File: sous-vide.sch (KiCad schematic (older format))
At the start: 25 parts, among them J2 Conn_01x02, J3 Conn_01x02, J5 Conn_01x02, Q1 2N3904, SW1 SW_Push_Dual, SW2 SW_Push_Dual, U1 node_mcu1.0, U2 RAC01, U3 G5LE, U4 LCD_Backpack, U5 P090S-04F20BR10K

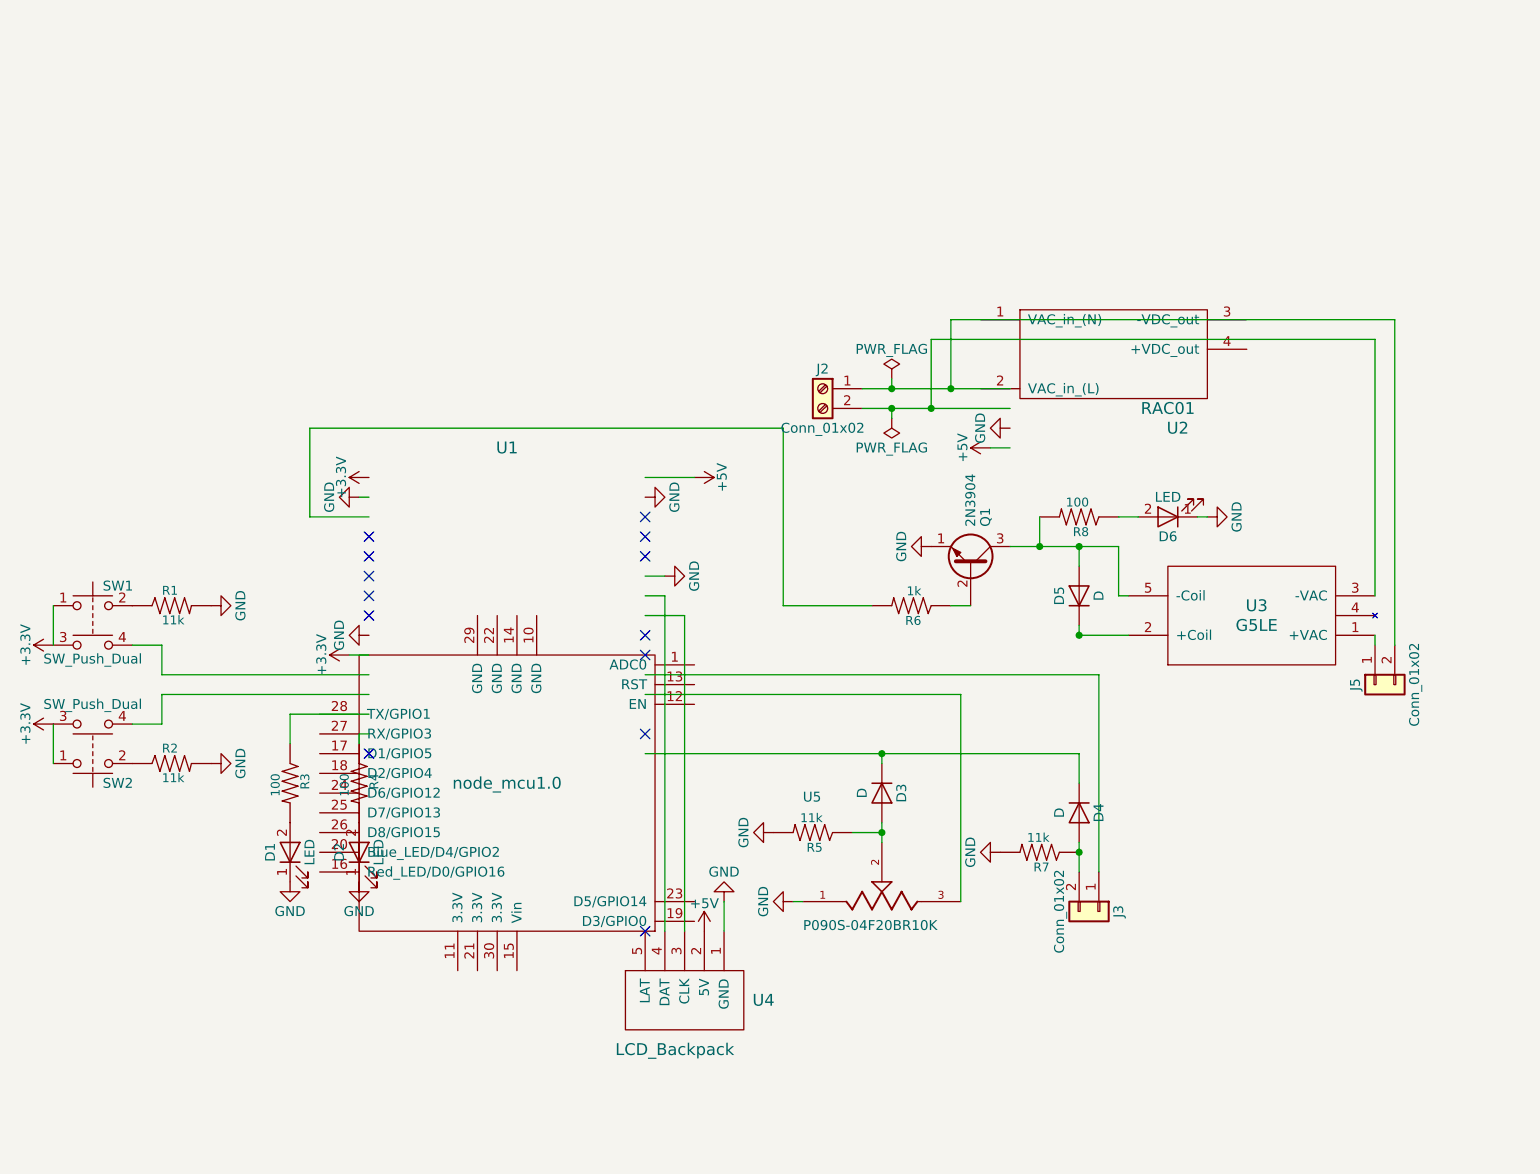
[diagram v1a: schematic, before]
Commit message: started testing pins for GPIO
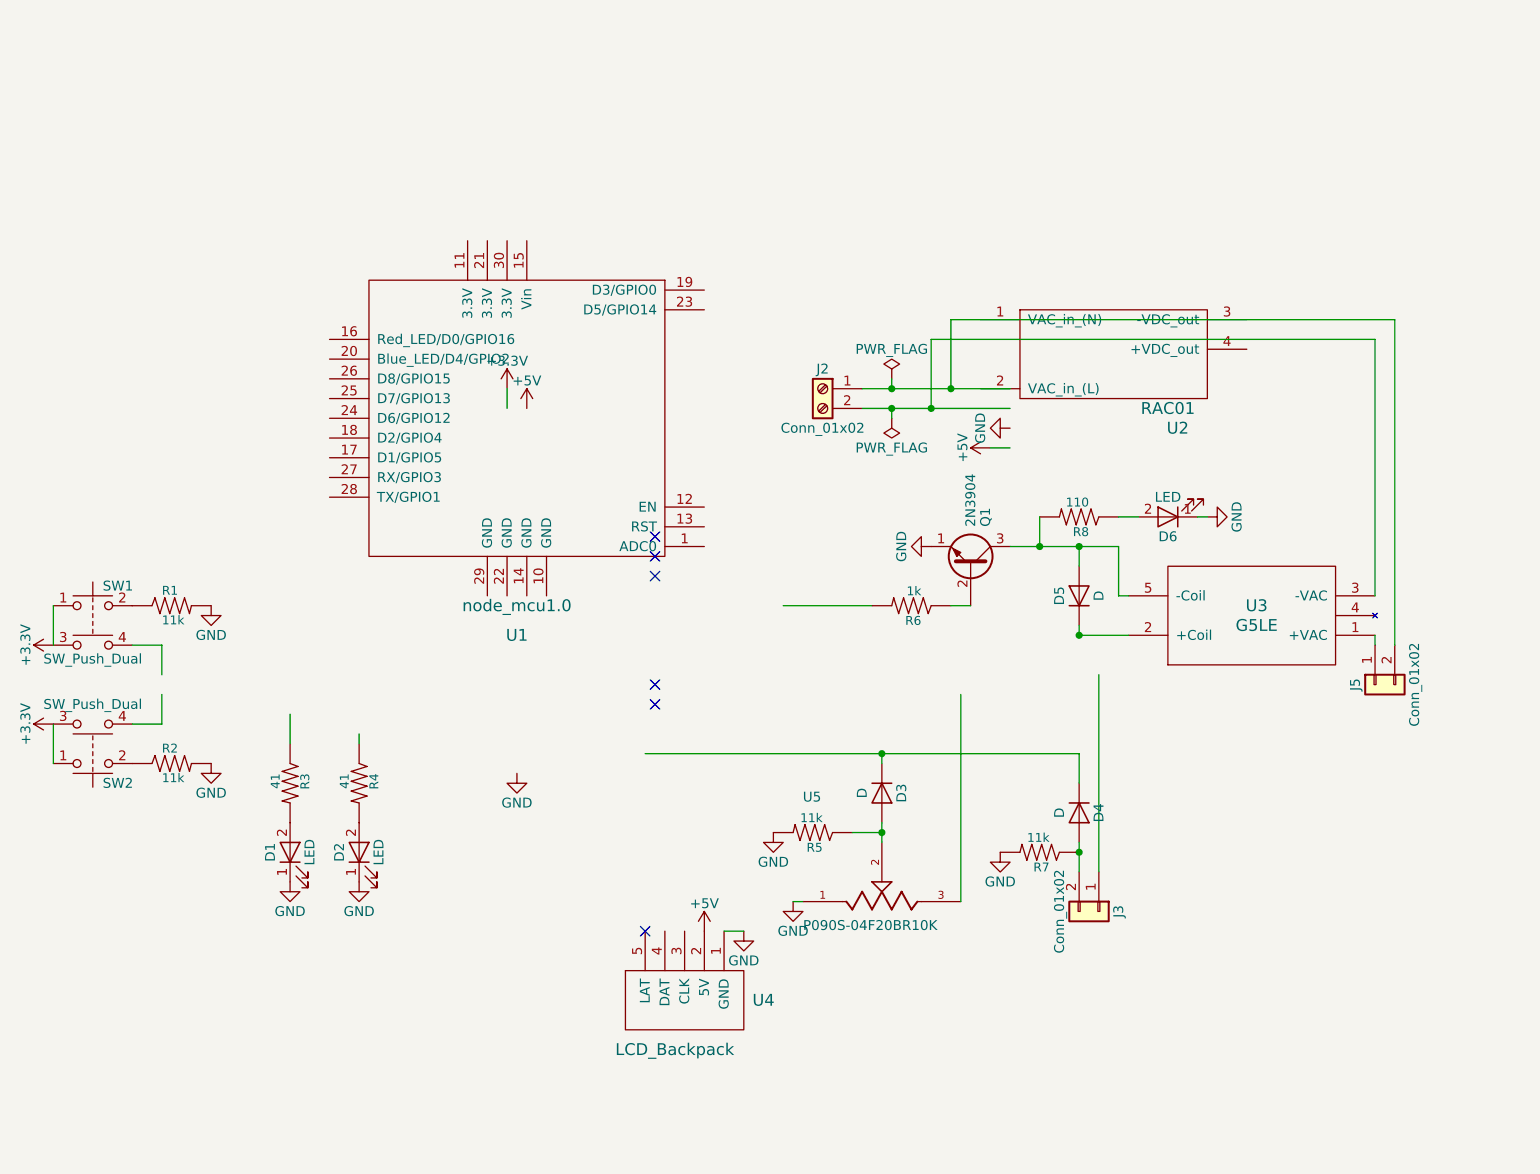
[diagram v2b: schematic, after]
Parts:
- R3, R4: value 100 -> 41
- R8: value 100 -> 110
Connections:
- wire segments 60 -> 43
- no-connect marks 13 -> 6
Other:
- moved on the sheet: U1
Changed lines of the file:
@@
 L GND #PWR01
 U 1 1 5A456926
-P 5050 5200
-F 0 "#PWR01" H 5050 4950 50  0001 C CNN
-F 1 "GND" H 5050 5050 50  0000 C CNN
-F 2 "" H 5050 5200 50  0001 C CNN
-F 3 "" H 5050 5200 50  0001 C CNN
-	1    5050 5200
-	-1   0    0    1
+P 5150 5350
+F 0 "#PWR01" H 5150 5100 50  0001 C CNN
+F 1 "GND" H 5150 5200 50  0000 C CNN
+F 2 "" H 5150 5350 50  0001 C CNN
+F 3 "" H 5150 5350 50  0001 C CNN
+	1    5150 5350
+	1    0    0    -1
 $EndComp
 $Comp
 L node_mcu1.0 U1
 U 1 1 5A457536
-P 3950 4650
-F 0 "U1" H 3950 2900 60  0000 C CNN
-F 1 "node_mcu1.0" H 3950 4600 60  0000 C CNN
-F 2 "custom:NodeMCU_1_0" H 3700 4600 60  0001 C CNN
-F 3 "" H 3700 4600 60  0001 C CNN
-	1    3950 4650
-	-1   0    0    1
+P 4000 2750
+F 0 "U1" H 4000 1650 60  0000 C CNN
+F 1 "node_mcu1.0" H 4000 1800 60  0000 C CNN
+F 2 "custom:NodeMCU_1_0" H 3750 2700 60  0001 C CNN
+F 3 "" H 3750 2700 60  0001 C CNN
+	1    4000 2750
+	-1   0    0    -1
 $EndComp
 $Comp
@@
 F 3 "" H 5400 5200 50  0001 C CNN
 	1    5400 5200
-	0    1    1    0
+	1    0    0    -1
 $EndComp
 $Comp
@@
 F 3 "" H 5300 4850 50  0001 C CNN
 	1    5300 4850
-	0    1    1    0
+	1    0    0    -1
 $EndComp
 $Comp
@@
 F 3 "" H 6450 4950 50  0001 C CNN
 	1    6450 4950
-	0    1    1    0
+	1    0    0    -1
 $EndComp
 $Comp
@@
 $EndComp
 Wire Wire Line
-	6950 4050 4650 4050
-Wire Wire Line
-	2950 2800 2950 3250
-Wire Wire Line
-	2950 3250 3250 3250
-Wire Wire Line
 	6850 4900 6850 5050
-Wire Wire Line
-	4650 4150 6250 4150
-Wire Wire Line
-	4750 5350 4750 3650
-Wire Wire Line
-	4750 3650 4650 3650
-Wire Wire Line
-	4850 5350 4850 3750
-Wire Wire Line
-	4850 3750 4650 3750
 Wire Wire Line
 	6850 4950 6850 4950
@@
 	0    1    1    0
 $EndComp
-Wire Wire Line
-	5350 2800 2950 2800
-Wire Wire Line
-	5350 2800 5350 3700
 Wire Wire Line
 	6500 3400 7050 3400
@@
 F 3 "" H 2450 4500 50  0001 C CNN
 	1    2450 4500
-	0    -1   -1   0
+	1    0    0    -1
 $EndComp
 Wire Wire Line
@@
 P 6850 3250
 F 0 "R8" H 6800 3300 45  0000 L BNN
-F 1 "100" H 6800 3150 45  0000 L BNN
+F 1 "110" H 6800 3150 45  0000 L BNN
 F 2 "Resistors_THT:R_Axial_DIN0204_L3.6mm_D1.6mm_P7.62mm_Horizontal" H 6850 3400 20  0001 C CNN
 F 3 "" H 6850 3250 60  0001 C CNN
@@
 P 3200 4600
 F 0 "R4" H 3150 4650 45  0000 L BNN
-F 1 "100" H 3150 4500 45  0000 L BNN
+F 1 "41" H 3150 4500 45  0000 L BNN
 F 2 "Resistors_THT:R_Axial_DIN0204_L3.6mm_D1.6mm_P7.62mm_Horizontal" H 3200 4750 20  0001 C CNN
 F 3 "" H 3200 4600 60  0001 C CNN
@@
 Wire Wire Line
 	3200 4400 3200 4350
-Wire Wire Line
-	3200 4350 3250 4350
 $Comp
 L RESISTOR0402 R2
@@
 F 3 "" H 2450 3700 50  0001 C CNN
 	1    2450 3700
-	0    -1   -1   0
+	1    0    0    -1
 $EndComp
 Wire Wire Line
@@
 Wire Wire Line
 	2200 4300 2200 4150
-Wire Wire Line
-	2200 4150 3250 4150
-Wire Wire Line
-	2200 4050 3250 4050
 $Comp
 L RESISTOR0402 R3
@@
 P 2850 4600
 F 0 "R3" H 2800 4650 45  0000 L BNN
-F 1 "100" H 2800 4500 45  0000 L BNN
+F 1 "41" H 2800 4500 45  0000 L BNN
 F 2 "Resistors_THT:R_Axial_DIN0204_L3.6mm_D1.6mm_P7.62mm_Horizontal" H 2850 4750 20  0001 C CNN
 F 3 "" H 2850 4600 60  0001 C CNN
@@
 	2850 4400 2850 4250
 Wire Wire Line
-	2850 4250 3250 4250
-Wire Wire Line
 	8350 3900 8350 3850
 Wire Wire Line
@@
 Connection ~ 6100 2700
 Connection ~ 6200 2600
-NoConn ~ 3250 4450
-NoConn ~ 3250 3750
-NoConn ~ 3250 3650
-NoConn ~ 3250 3550
-NoConn ~ 3250 3450
-NoConn ~ 3250 3350
-NoConn ~ 4650 3250
-NoConn ~ 4650 3350
-NoConn ~ 4650 3450
-$Comp
-L GND #PWR011
-U 1 1 5A4713DB
-P 4750 3550
-F 0 "#PWR011" H 4750 3300 50  0001 C CNN
-F 1 "GND" H 4750 3400 50  0000 C CNN
-F 2 "" H 4750 3550 50  0001 C CNN
-F 3 "" H 4750 3550 50  0001 C CNN
-	1    4750 3550
-	0    -1   -1   0
-$EndComp
-$Comp
-L GND #PWR012
-U 1 1 5A471499
-P 3200 3150
-F 0 "#PWR012" H 3200 2900 50  0001 C CNN
-F 1 "GND" H 3200 3000 50  0000 C CNN
-F 2 "" H 3200 3150 50  0001 C CNN
-F 3 "" H 3200 3150 50  0001 C CNN
-	1    3200 3150
-	0    1    1    0
-$EndComp
-NoConn ~ 4650 3850
-NoConn ~ 4650 3950
-NoConn ~ 4650 4350
-Wire Wire Line
-	4650 3550 4750 3550
-Wire Wire Line
-	3250 3150 3200 3150
 $Comp
 L GND #PWR013
@@
 F 3 "" H 6500 2800 50  0001 C CNN
 	1    6500 2800
-	0    1    1    0
-$EndComp
-$Comp
-L GND #PWR014
-U 1 1 5A475347
-P 4650 3150
-F 0 "#PWR014" H 4650 2900 50  0001 C CNN
-F 1 "GND" H 4650 3000 50  0000 C CNN
-F 2 "" H 4650 3150 50  0001 C CNN
-F 3 "" H 4650 3150 50  0001 C CNN
-	1    4650 3150
-	0    -1   -1   0
-$EndComp
-Wire Wire Line
-	4650 3050 4900 3050
-$Comp
-L GND #PWR015
-U 1 1 5A478DA6
-P 3250 3850
-F 0 "#PWR015" H 3250 3600 50  0001 C CNN
-F 1 "GND" H 3250 3700 50  0000 C CNN
-F 2 "" H 3250 3850 50  0001 C CNN
-F 3 "" H 3250 3850 50  0001 C CNN
-	1    3250 3850
 	0    1    1    0
 $EndComp
@@
 $EndComp
 $Comp
-L +5V #PWR018
-U 1 1 5A46409D
-P 4900 3050
-F 0 "#PWR018" H 4900 2900 50  0001 C CNN
-F 1 "+5V" H 4900 3190 50  0000 C CNN
-F 2 "" H 4900 3050 50  0001 C CNN
-F 3 "" H 4900 3050 50  0001 C CNN
-	1    4900 3050
-	0    1    1    0
-$EndComp
-$Comp
 L +5V #PWR019
 U 1 1 5A4640F9
@@
 $EndComp
 Wire Wire Line
-	5050 5200 5050 5350
+	5150 5350 5050 5350
 Connection ~ 5900 2600
 $Comp
@@
 Wire Wire Line
 	1650 4300 1650 4500
-$Comp
-L +3.3V #PWR023
-U 1 1 5A476C4E
-P 3250 3050
-F 0 "#PWR023" H 3250 2900 50  0001 C CNN
-F 1 "+3.3V" H 3250 3190 50  0000 C CNN
-F 2 "" H 3250 3050 50  0001 C CNN
-F 3 "" H 3250 3050 50  0001 C CNN
-	1    3250 3050
-	0    -1   -1   0
-$EndComp
-$Comp
-L +3.3V #PWR024
-U 1 1 5A4637BE
-P 3150 3950
-F 0 "#PWR024" H 3150 3800 50  0001 C CNN
-F 1 "+3.3V" H 3150 4090 50  0000 C CNN
-F 2 "" H 3150 3950 50  0001 C CNN
-F 3 "" H 3150 3950 50  0001 C CNN
-	1    3150 3950
-	0    -1   -1   0
-$EndComp
-Wire Wire Line
-	3150 3950 3250 3950
 $Comp
 L P090S-04F20BR10K U5
@@
 	1    0    0    -1
 $EndComp
+$Comp
+L +5V #PWR?
+U 1 1 5A48311D
+P 4050 2700
+F 0 "#PWR?" H 4050 2550 50  0001 C CNN
+F 1 "+5V" H 4050 2840 50  0000 C CNN
+F 2 "" H 4050 2700 50  0001 C CNN
+F 3 "" H 4050 2700 50  0001 C CNN
+	1    4050 2700
+	1    0    0    -1
+$EndComp
+$Comp
+L +3.3V #PWR?
+U 1 1 5A483163
+P 3950 2600
+F 0 "#PWR?" H 3950 2450 50  0001 C CNN
+F 1 "+3.3V" H 3950 2740 50  0000 C CNN
+F 2 "" H 3950 2600 50  0001 C CNN
+F 3 "" H 3950 2600 50  0001 C CNN
+	1    3950 2600
+	1    0    0    -1
+$EndComp
+Wire Wire Line
+	3950 2600 3950 2700
+$Comp
+L GND #PWR?
+U 1 1 5A48356C
+P 4000 4550
+F 0 "#PWR?" H 4000 4300 50  0001 C CNN
+F 1 "GND" H 4000 4400 50  0000 C CNN
+F 2 "" H 4000 4550 50  0001 C CNN
+F 3 "" H 4000 4550 50  0001 C CNN
+	1    4000 4550
+	1    0    0    -1
+$EndComp
+NoConn ~ 4700 4100
+NoConn ~ 4700 4200
+NoConn ~ 4700 3350
+NoConn ~ 4700 3450
+NoConn ~ 4700 3550
 $EndSCHEMATC

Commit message: redo entire schematic and layout
now complete with danger zone!
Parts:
- removed R1, R2: 11k, Resistors_THT:R_Axial_DIN0204_L3.6mm_D1.6mm_P7.62mm_Horizontal, symbol RESISTOR0402
- renumbered D3 to D1, D5 to D2, D6 to D3, D2 to D5, D1 to D6, J5 to J1, R8 to R1, R5 to R2, R6 to R3, R3 to R5, R7 to R6, U3 to U1, U1 to U3, U5 to U4, U4 to U5
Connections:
- net labels added: A0, BLUE_LED, CLK, DAT, RED_LED, SW1, SW2, THERMISTOR, UESR_POT
- wire segments 43 -> 60
- no-connect marks 6 -> 9
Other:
- note added: "Danger Zone"
- moved on the sheet: D1, D2, D3, D4, D5, D6, J1, J2, J3, Q1, R1, R2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

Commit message: fix DRC issues
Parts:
- U4: value P090S-04F20BR10K -> P090S
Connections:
- net labels removed: +3.3V
- wire segments 60 -> 44
- no-connect marks 9 -> 12
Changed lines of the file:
@@
 P 6500 5900
 F 0 "U4" H 6250 5950 50  0000 L BNN
-F 1 "P090S-04F20BR10K" H 6100 5750 50  0000 L BNN
+F 1 "P090S" H 6100 5750 50  0000 L BNN
 F 2 "P090S-04F20BR10K:TRIM_P090S-04F20BR10K" H 6500 5900 50  0001 L BNN
 F 3 "P090S-04F20BR10K" H 6500 5900 50  0001 L BNN
@@
 $EndComp
 $Comp
-L node_mcu1.0 U3
-U 1 1 5A457536
-P 5400 4200
-F 0 "U3" H 5250 4050 60  0000 C CNN
-F 1 "node_mcu1.0" H 5250 4200 60  0000 C CNN
-F 2 "custom:NodeMCU_1_0" H 5150 4150 60  0001 C CNN
-F 3 "" H 5150 4150 60  0001 C CNN
-	1    5400 4200
-	1    0    0    -1
-$EndComp
-$Comp
 L GND #PWR014
 U 1 1 5A485E99
@@
 NoConn ~ 6350 4500
 $Comp
-L +3.3V #PWR016
-U 1 1 5A483163
-P 5450 3250
-F 0 "#PWR016" H 5450 3100 50  0001 C CNN
-F 1 "+3.3V" H 5450 3390 50  0000 C CNN
-F 2 "" H 5450 3250 50  0001 C CNN
-F 3 "" H 5450 3250 50  0001 C CNN
-	1    5450 3250
-	1    0    0    -1
-$EndComp
-$Comp
-L +5V #PWR017
+L +5V #PWR016
 U 1 1 5A490EFE
 P 5200 3300
-F 0 "#PWR017" H 5200 3150 50  0001 C CNN
+F 0 "#PWR016" H 5200 3150 50  0001 C CNN
 F 1 "+5V" H 5200 3440 50  0000 C CNN
 F 2 "" H 5200 3300 50  0001 C CNN
@@
 $EndComp
 $Comp
-L +5V #PWR018
+L +5V #PWR017
 U 1 1 5A491092
 P 6050 1300
-F 0 "#PWR018" H 6050 1150 50  0001 C CNN
+F 0 "#PWR017" H 6050 1150 50  0001 C CNN
 F 1 "+5V" H 6050 1440 50  0000 C CNN
 F 2 "" H 6050 1300 50  0001 C CNN
@@
 $EndComp
 $Comp
-L +5V #PWR019
+L +5V #PWR018
 U 1 1 5A4912B7
 P 7800 3800
-F 0 "#PWR019" H 7800 3650 50  0001 C CNN
+F 0 "#PWR018" H 7800 3650 50  0001 C CNN
 F 1 "+5V" H 7800 3940 50  0000 C CNN
 F 2 "" H 7800 3800 50  0001 C CNN
@@
 Text Label 4250 3550 0    60   ~ 0
 SW1
-Text Label 4250 4150 0    60   ~ 0
+Text Label 4250 3950 3    60   ~ 0
 SW2
 Wire Wire Line
-	6950 5450 7200 5450
-Wire Wire Line
-	7200 5450 7300 5450
+	6950 5450 7300 5450
 Connection ~ 7200 5450
 Wire Wire Line
 	5600 1400 6050 1400
 Wire Wire Line
-	6050 1300 6050 1400
-Wire Wire Line
-	6050 1400 6050 1450
-Wire Wire Line
-	5650 1850 6050 1850
-Wire Wire Line
-	6050 1850 6250 1850
-Wire Wire Line
-	6050 1750 6050 1850
-Wire Wire Line
-	6050 1850 6050 1900
+	6050 1300 6050 1450
+Wire Wire Line
+	5650 1850 6250 1850
+Wire Wire Line
+	6050 1750 6050 1900
 Connection ~ 6050 1400
 Wire Wire Line
@@
 	3650 2150 3650 2200
 Wire Wire Line
-	6100 5900 6150 5900
-Wire Wire Line
-	6150 5900 6200 5900
-Wire Wire Line
-	5450 3300 5450 3250
+	6100 5900 6200 5900
 Wire Wire Line
 	3550 3550 3700 3550
@@
 Wire Wire Line
 	4100 3550 4450 3550
-Wire Wire Line
-	4450 3550 4450 3700
-Wire Wire Line
-	4450 3800 4450 4150
-Wire Wire Line
-	4450 4150 4100 4150
 Wire Wire Line
 	6350 3550 6350 3800
@@
 Connection ~ 6150 5900
 Wire Wire Line
-	4450 5450 5800 5450
-Wire Wire Line
-	5800 5450 6650 5450
+	4450 5450 6650 5450
 Wire Wire Line
 	4450 5450 4450 4850
@@
 	6450 4000 6350 4000
 Wire Wire Line
-	3500 2200 3650 2200
-Wire Wire Line
-	3650 2200 4000 2200
-Wire Wire Line
-	4000 2200 4350 2200
+	3500 2200 4350 2200
 Wire Wire Line
 	4000 2200 4000 1500
 Wire Wire Line
-	4200 1600 4200 2300
-Wire Wire Line
-	4200 2300 4200 2550
+	4200 1600 4200 2550
 Wire Wire Line
 	4200 1600 4350 1600
 Wire Wire Line
-	3500 2300 3650 2300
-Wire Wire Line
-	3650 2300 4200 2300
+	3500 2300 4200 2300
 Wire Wire Line
 	3500 1400 4350 1400
@@
 UESR_POT
 Wire Wire Line
-	5450 3300 5550 3300
-Wire Wire Line
-	5550 3300 5650 3300
-Connection ~ 5550 3300
-Wire Wire Line
-	5250 5100 5350 5100
-Wire Wire Line
-	5350 5100 5400 5100
-Wire Wire Line
-	5400 5100 5450 5100
-Wire Wire Line
-	5450 5100 5550 5100
+	5250 5100 5550 5100
 Connection ~ 5350 5100
 Connection ~ 5400 5100
 Connection ~ 5450 5100
+Wire Wire Line
+	4100 4150 4250 4150
+Wire Wire Line
+	4250 4150 4250 3650
+Wire Wire Line
+	4250 3650 4450 3650
+$Comp
+L node_mcu1.0 U3
+U 1 1 5A457536
+P 5400 4200
+F 0 "U3" H 5250 4050 60  0000 C CNN
+F 1 "node_mcu1.0" H 5250 4200 60  0000 C CNN
+F 2 "custom:NodeMCU_1_0" H 5150 4150 60  0001 C CNN
+F 3 "" H 5150 4150 60  0001 C CNN
+	1    5400 4200
+	1    0    0    -1
+$EndComp
+NoConn ~ 5450 3300
+NoConn ~ 5550 3300
+NoConn ~ 5650 3300
 $EndSCHEMATC

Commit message: fix resistor footprints
 - add dashed line
 - fix pot to use through hole mounting
 - checked everything for footprint errors
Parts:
- R1, R2, R6: footprint Resistors_THT:R_Axial_DIN0204_L3.6mm_D1.6mm_P7.62mm_Horizontal -> Resistors_THT:R_Axial_DIN0207_L6.3mm_D2.5mm_P10.16mm_Horizontal
- R3: value 1k -> 1.1k; footprint Resistors_THT:R_Axial_DIN0204_L3.6mm_D1.6mm_P7.62mm_Horizontal -> Resistors_THT:R_Axial_DIN0207_L6.3mm_D2.5mm_P10.16mm_Horizontal
- R4, R5: value 41 -> 43; footprint Resistors_THT:R_Axial_DIN0204_L3.6mm_D1.6mm_P7.62mm_Horizontal -> Resistors_THT:R_Axial_DIN0207_L6.3mm_D2.5mm_P10.16mm_Horizontal
- U4: footprint P090S-04F20BR10K:TRIM_P090S-04F20BR10K -> custom:P090S-THT_MNT
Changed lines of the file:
@@
 F 0 "R2" H 6100 6150 45  0000 L BNN
 F 1 "11k" H 6100 6000 45  0000 L BNN
-F 2 "Resistors_THT:R_Axial_DIN0204_L3.6mm_D1.6mm_P7.62mm_Horizontal" H 6150 6250 20  0001 C CNN
+F 2 "Resistors_THT:R_Axial_DIN0207_L6.3mm_D2.5mm_P10.16mm_Horizontal" H 6150 6250 20  0001 C CNN
 F 3 "" H 6150 6100 60  0001 C CNN
 F 4 " " H 6150 6300 60  0000 C CNN "Field4"
@@
 F 0 "R6" H 7150 5700 45  0000 L BNN
 F 1 "11k" H 7150 5550 45  0000 L BNN
-F 2 "Resistors_THT:R_Axial_DIN0204_L3.6mm_D1.6mm_P7.62mm_Horizontal" H 7200 5800 20  0001 C CNN
+F 2 "Resistors_THT:R_Axial_DIN0207_L6.3mm_D2.5mm_P10.16mm_Horizontal" H 7200 5800 20  0001 C CNN
 F 3 "" H 7200 5650 60  0001 C CNN
 F 4 " " H 7200 5850 60  0000 C CNN "Field4"
@@
 P 6450 2350
 F 0 "R3" H 6400 2400 45  0000 L BNN
-F 1 "1k" H 6400 2250 45  0000 L BNN
-F 2 "Resistors_THT:R_Axial_DIN0204_L3.6mm_D1.6mm_P7.62mm_Horizontal" H 6450 2500 20  0001 C CNN
+F 1 "1.1k" H 6400 2250 45  0000 L BNN
+F 2 "Resistors_THT:R_Axial_DIN0207_L6.3mm_D2.5mm_P10.16mm_Horizontal" H 6450 2500 20  0001 C CNN
 F 3 "" H 6450 2350 60  0001 C CNN
 F 4 " " H 6450 2550 60  0000 C CNN "Field4"
@@
 F 0 "R1" H 6000 2150 45  0000 L BNN
 F 1 "110" H 6000 2000 45  0000 L BNN
-F 2 "Resistors_THT:R_Axial_DIN0204_L3.6mm_D1.6mm_P7.62mm_Horizontal" H 6050 2250 20  0001 C CNN
+F 2 "Resistors_THT:R_Axial_DIN0207_L6.3mm_D2.5mm_P10.16mm_Horizontal" H 6050 2250 20  0001 C CNN
 F 3 "" H 6050 2100 60  0001 C CNN
 F 4 " " H 6050 2300 60  0000 C CNN "Field4"
@@
 P 7050 3550
 F 0 "R4" H 7000 3600 45  0000 L BNN
-F 1 "41" H 7000 3450 45  0000 L BNN
-F 2 "Resistors_THT:R_Axial_DIN0204_L3.6mm_D1.6mm_P7.62mm_Horizontal" H 7050 3700 20  0001 C CNN
+F 1 "43" H 7000 3450 45  0000 L BNN
+F 2 "Resistors_THT:R_Axial_DIN0207_L6.3mm_D2.5mm_P10.16mm_Horizontal" H 7050 3700 20  0001 C CNN
 F 3 "" H 7050 3550 60  0001 C CNN
 F 4 " " H 7050 3750 60  0000 C CNN "Field4"
@@
 P 7100 3900
 F 0 "R5" H 7050 3950 45  0000 L BNN
-F 1 "41" H 7050 3800 45  0000 L BNN
-F 2 "Resistors_THT:R_Axial_DIN0204_L3.6mm_D1.6mm_P7.62mm_Horizontal" H 7100 4050 20  0001 C CNN
+F 1 "43" H 7050 3800 45  0000 L BNN
+F 2 "Resistors_THT:R_Axial_DIN0207_L6.3mm_D2.5mm_P10.16mm_Horizontal" H 7100 4050 20  0001 C CNN
 F 3 "" H 7100 3900 60  0001 C CNN
 F 4 " " H 7100 4100 60  0000 C CNN "Field4"
@@
 F 0 "U4" H 6250 5950 50  0000 L BNN
 F 1 "P090S" H 6100 5750 50  0000 L BNN
-F 2 "P090S-04F20BR10K:TRIM_P090S-04F20BR10K" H 6500 5900 50  0001 L BNN
+F 2 "custom:P090S-THT_MNT" H 6500 5900 50  0001 L BNN
 F 3 "P090S-04F20BR10K" H 6500 5900 50  0001 L BNN
 F 4 "Good" H 6500 5900 50  0001 L BNN "Field4"
